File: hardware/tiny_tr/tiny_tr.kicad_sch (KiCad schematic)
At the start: 10 parts, among them U1 ATtiny85-20P, U2 PAM8302AAD

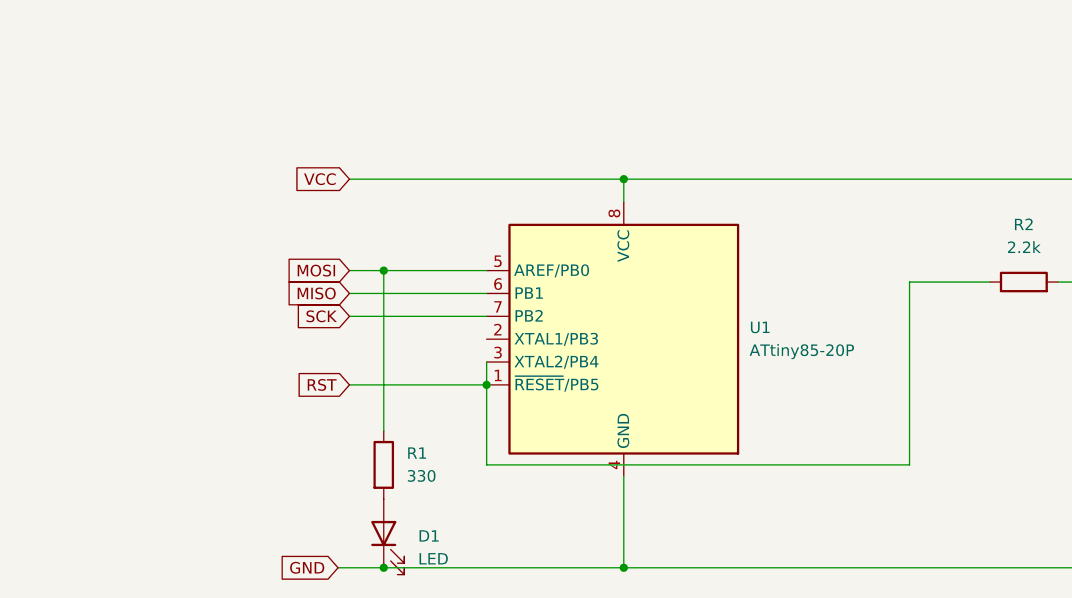
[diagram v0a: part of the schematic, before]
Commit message: feat(hardware): Create schematic based on current circuit
Co-Authored-By: Claude Sonnet 4.5 <noreply@anthropic.com>
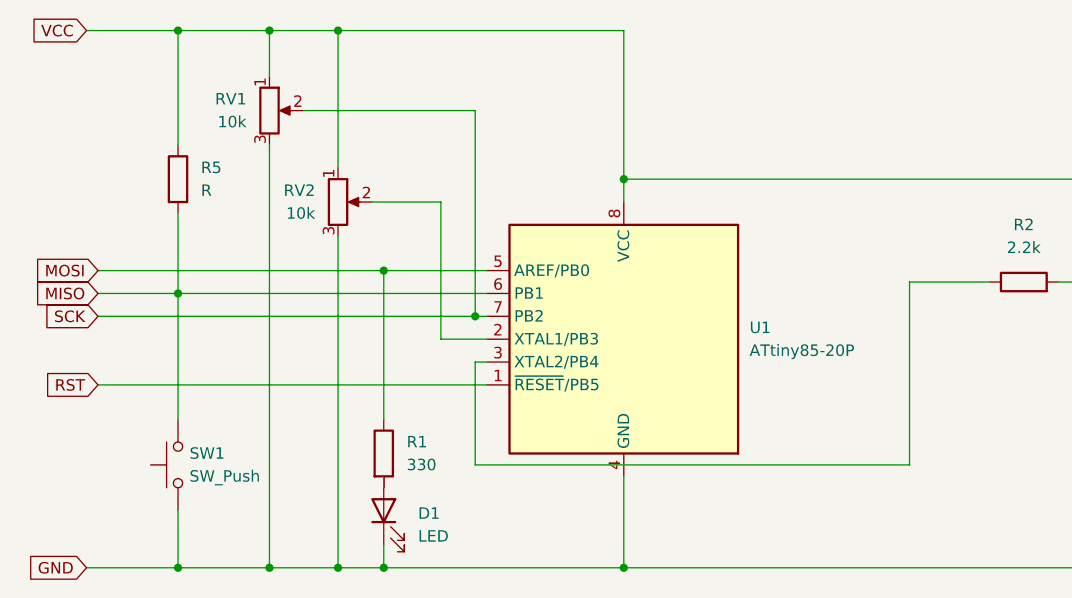
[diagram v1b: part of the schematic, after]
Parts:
- added R5: R, symbol Device:R
- added RV1, RV2: 10k, symbol Device:R_Potentiometer
- added SW1: SW_Push, symbol Switch:SW_Push
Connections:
- net GND: now also RV1.3, RV2.3, SW1.1
- net MISO: now also R5.2, SW1.2
- net RST: no longer R2.1, U1.3 (XTAL2/PB4)
- net SCK: now also RV1.2
- net VCC: now also R5.1, RV1.1, RV2.1
- net at U1.2 (XTAL1/PB3): now also RV2.2
- new net: R2.1, U1.3 (XTAL2/PB4)
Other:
- moved on the sheet: D1, R1

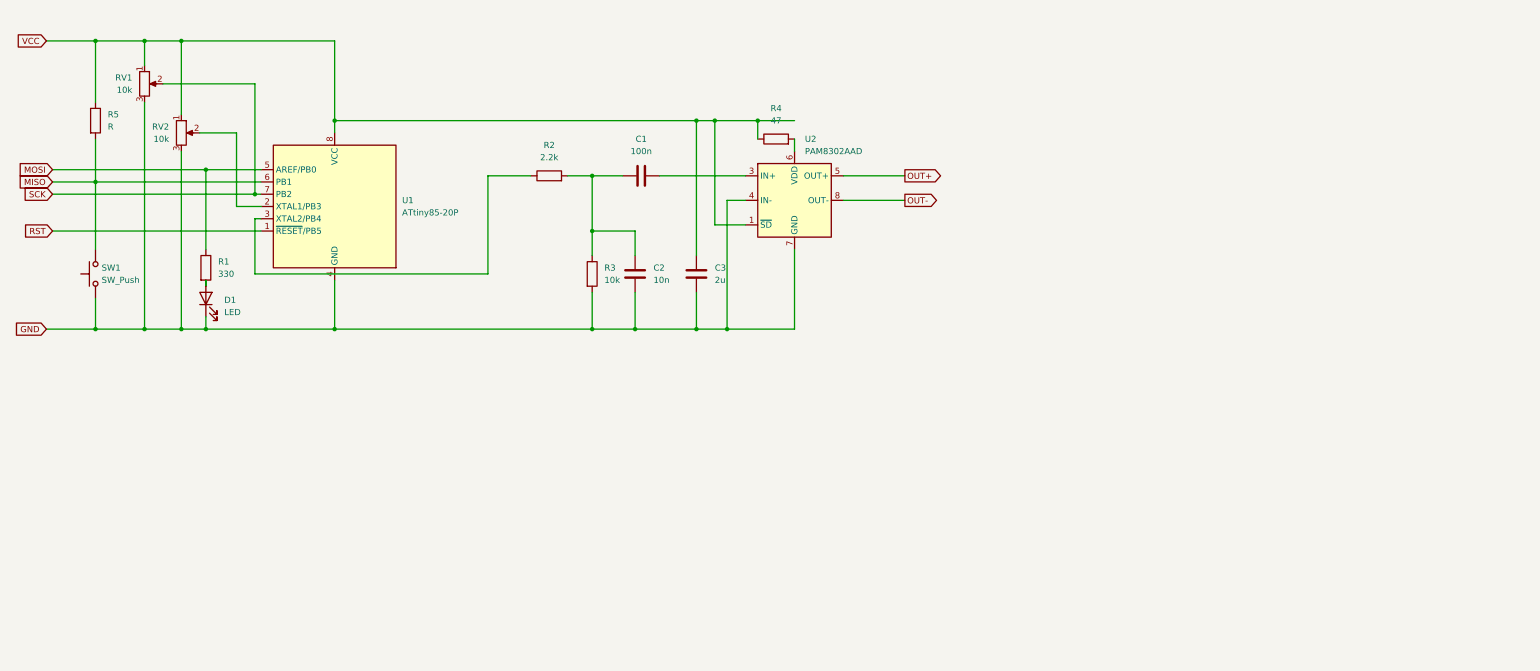
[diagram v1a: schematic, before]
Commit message: fix(hardware): Update capacitor values for noise reduction
Co-Authored-By: Claude Opus 4.5 <noreply@anthropic.com>
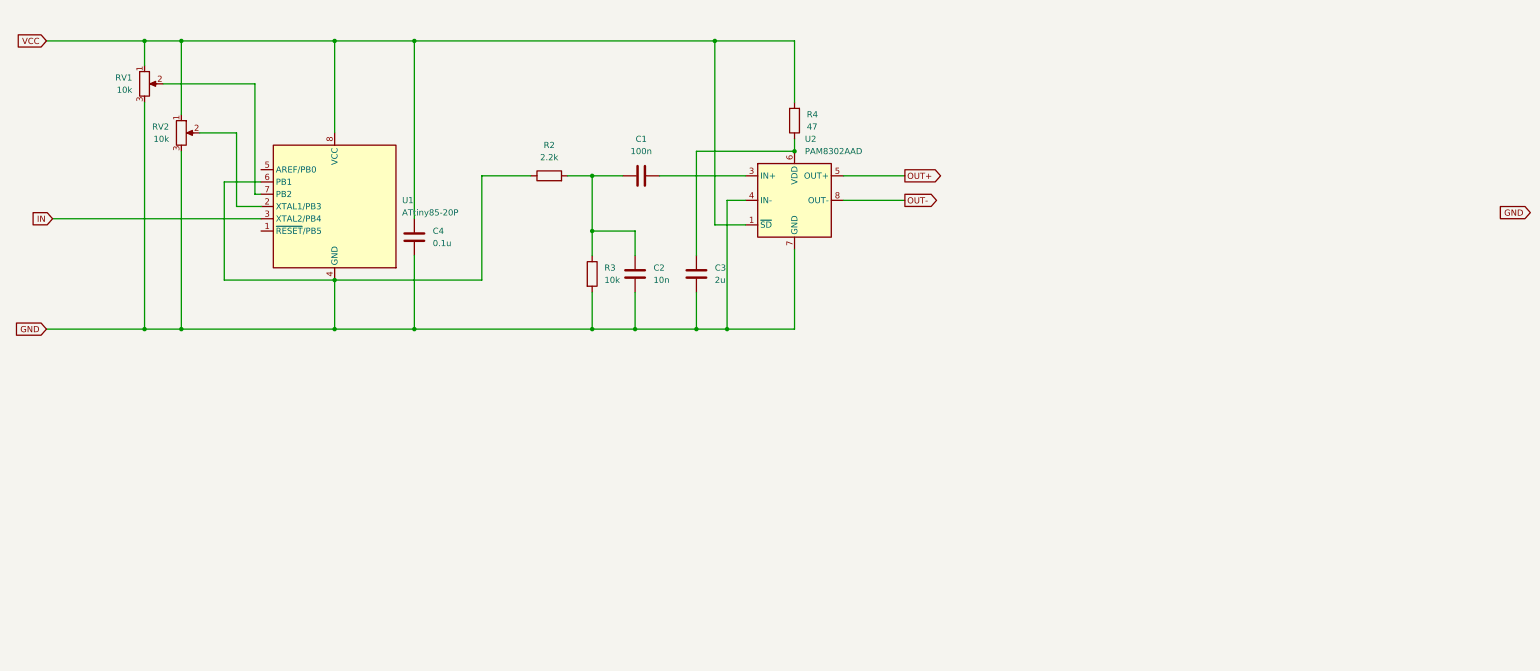
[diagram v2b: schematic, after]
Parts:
- removed D1: LED, symbol Device:LED
- removed R1: 330, symbol Device:R
- removed R5: R, symbol Device:R
- removed SW1: SW_Push, symbol Switch:SW_Push
- added C4: 0.1u, symbol Device:C
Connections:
- net MISO is gone; now on net GND: U1.6 (PB1)
- net GND: now also R2.1, C4.2
- net VCC: now also R4.2, C4.1; no longer C3.1, R4.1
- net IN: now reaches U1.3 (XTAL2/PB4)
- net IN: no longer R2.1
- net at U2.6 (VDD): now also C3.1, R4.1; no longer R4.2
- net MOSI: no longer names the net of U1.5 (AREF/PB0)
- net RST: no longer names the net of U1.1 (~{RESET}/PB5)
- net SCK: no longer names the net of RV1.2, U1.7 (PB2)
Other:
- moved on the sheet: R4

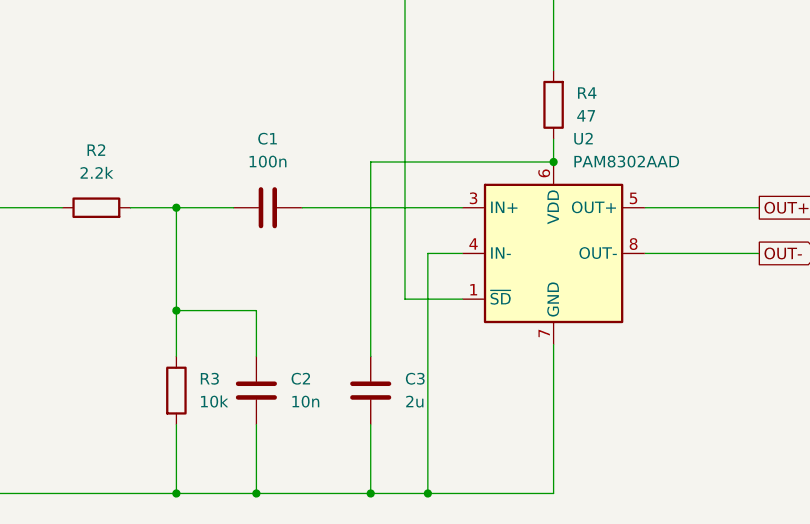
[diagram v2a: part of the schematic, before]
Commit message: fix(hardware): Increase PAM8302 bypass capacitor to 100uF
Prevents voltage droop during kick attack that was causing
power rail fluctuations.

Co-Authored-By: Claude Opus 4.5 <noreply@anthropic.com>
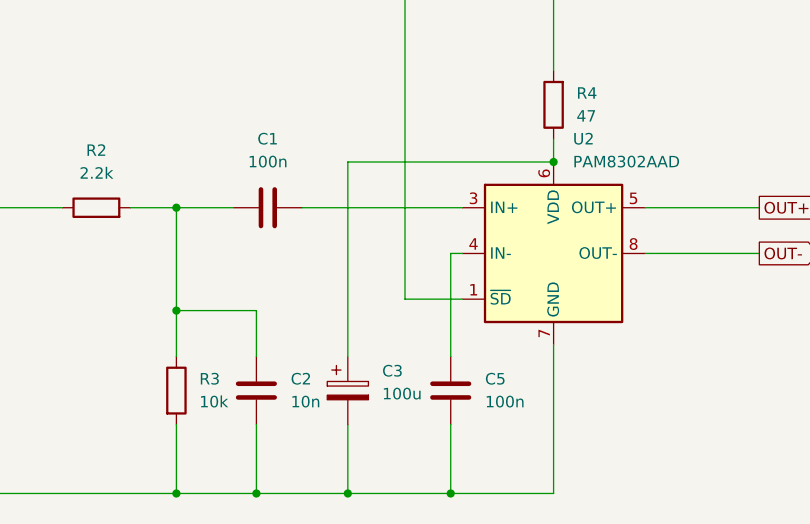
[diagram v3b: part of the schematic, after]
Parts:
- removed C3: 2u, symbol Device:C
- added C3: 100u, symbol Device:C_Polarized
- added C5: 100n, symbol Device:C
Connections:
- net GND: now also C3.2, C5.2; no longer U2.4 (IN-)
- net at R4.1, U2.6 (VDD): now also C3.1
- new net: C5.1, U2.4 (IN-)
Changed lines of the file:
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@@
-	)
-	(junction
-		(at 162.56 92.71)
-		(diameter 0)
-		(color 0 0 0 0)
 	)
 	(junction
@@
 	)
 	(junction
-		(at 156.21 92.71)
+		(at 41.91 33.02)
 		(diameter 0)
 		(color 0 0 0 0)
 	)
 	(junction
-		(at 41.91 33.02)
+		(at 165.1 92.71)
 		(diameter 0)
 		(color 0 0 0 0)
@@
 	)
 	(junction
+		(at 153.67 92.71)
+		(diameter 0)
+		(color 0 0 0 0)
+	)
+	(junction
 		(at 176.53 55.88)
 		(diameter 0)
@@
 	(wire
 		(pts
-			(xy 162.56 66.04) (xy 162.56 92.71)
+			(xy 165.1 66.04) (xy 165.1 77.47)
+		)
+		(stroke
+			(width 0)
+			(type default)
+		)
+	)
+	(wire
+		(pts
+			(xy 165.1 92.71) (xy 176.53 92.71)
 		)
 		(stroke
@@
 	(wire
 		(pts
-			(xy 156.21 85.09) (xy 156.21 92.71)
+			(xy 153.67 85.09) (xy 153.67 92.71)
 		)
 		(stroke
@@
 	(wire
 		(pts
+			(xy 153.67 55.88) (xy 153.67 77.47)
+		)
+		(stroke
+			(width 0)
+			(type default)
+		)
+	)
+	(wire
+		(pts
 			(xy 49.53 33.02) (xy 81.28 33.02)
 		)
@@
 	(wire
 		(pts
-			(xy 156.21 55.88) (xy 176.53 55.88)
+			(xy 153.67 55.88) (xy 176.53 55.88)
 		)
 		(stroke
@@
 	(wire
 		(pts
-			(xy 143.51 92.71) (xy 156.21 92.71)
+			(xy 143.51 92.71) (xy 153.67 92.71)
 		)
 		(stroke
@@
 	(wire
 		(pts
+			(xy 153.67 92.71) (xy 165.1 92.71)
+		)
+		(stroke
+			(width 0)
+			(type default)
+		)
+	)
+	(wire
+		(pts
 			(xy 97.79 33.02) (xy 97.79 69.85)
 		)
@@
 	(wire
 		(pts
-			(xy 166.37 66.04) (xy 162.56 66.04)
+			(xy 166.37 66.04) (xy 165.1 66.04)
 		)
 		(stroke
@@
 	(wire
 		(pts
+			(xy 165.1 85.09) (xy 165.1 92.71)
+		)
+		(stroke
+			(width 0)
+			(type default)
+		)
+	)
+	(wire
+		(pts
 			(xy 45.72 41.91) (xy 64.77 41.91)
 		)
@@
 	(wire
 		(pts
-			(xy 156.21 92.71) (xy 162.56 92.71)
-		)
-		(stroke
-			(width 0)
-			(type default)
-		)
-	)
-	(wire
-		(pts
-			(xy 162.56 92.71) (xy 176.53 92.71)
-		)
-		(stroke
-			(width 0)
-			(type default)
-		)
-	)
-	(wire
-		(pts
 			(xy 148.59 60.96) (xy 166.37 60.96)
-		)
-		(stroke
-			(width 0)
-			(type default)
-		)
-	)
-	(wire
-		(pts
-			(xy 156.21 55.88) (xy 156.21 77.47)
 		)
 		(stroke
@@
 	)
 	(symbol
+		(lib_id "Device:C")
+		(at 165.1 81.28 0)
+		(unit 1)
+		(exclude_from_sim no)
+		(in_bom yes)
+		(on_board yes)
+		(dnp no)
+		(fields_autoplaced yes)
+		(property "Reference" "C5"
+			(at 168.91 80.0099 0)
+			(effects
+				(font
+					(size 1.27 1.27)
+				)
+				(justify left)
+			)
+		)
+		(property "Value" "100n"
+			(at 168.91 82.5499 0)
+			(effects
+				(font
+					(size 1.27 1.27)
+				)
+				(justify left)
+			)
+		)
+		(property "Footprint" ""
+			(at 166.0652 85.09 0)
+			(effects
+				(font
+					(size 1.27 1.27)
+				)
+				(hide yes)
+			)
+		)
+		(property "Datasheet" "~"
+			(at 165.1 81.28 0)
+			(effects
+				(font
+					(size 1.27 1.27)
+				)
+				(hide yes)
+			)
+		)
+		(property "Description" "Unpolarized capacitor"
+			(at 165.1 81.28 0)
+			(effects
+				(font
+					(size 1.27 1.27)
+				)
+				(hide yes)
+			)
+		)
+		(pin "1"
+		)
+		(pin "2"
+		)
+		(instances
+			(project ""
+				(path "/b0a62a77-cbdd-43ac-b9b7-6d13322499f8"
+					(reference "C5")
+					(unit 1)
+				)
+			)
+		)
+	)
+	(symbol
 		(lib_id "Device:R")
 		(at 134.62 81.28 0)
@@
 				(path "/b0a62a77-cbdd-43ac-b9b7-6d13322499f8"
 					(reference "R3")
-					(unit 1)
-				)
-			)
-		)
-	)
-	(symbol
-		(lib_id "Device:C")
-		(at 156.21 81.28 0)
-		(unit 1)
-		(exclude_from_sim no)
-		(in_bom yes)
-		(on_board yes)
-		(dnp no)
-		(fields_autoplaced yes)
-		(property "Reference" "C3"
-			(at 160.02 80.0099 0)
-			(effects
-				(font
-					(size 1.27 1.27)
-				)
-				(justify left)
-			)
-		)
-		(property "Value" "2u"
-			(at 160.02 82.5499 0)
-			(effects
-				(font
-					(size 1.27 1.27)
-				)
-				(justify left)
-			)
-		)
-		(property "Footprint" ""
-			(at 157.1752 85.09 0)
-			(effects
-				(font
-					(size 1.27 1.27)
-				)
-				(hide yes)
-			)
-		)
-		(property "Datasheet" "~"
-			(at 156.21 81.28 0)
-			(effects
-				(font
-					(size 1.27 1.27)
-				)
-				(hide yes)
-			)
-		)
-		(property "Description" "Unpolarized capacitor"
-			(at 156.21 81.28 0)
-			(effects
-				(font
-					(size 1.27 1.27)
-				)
-				(hide yes)
-			)
-		)
-		(pin "1"
-		)
-		(pin "2"
-		)
-		(instances
-			(project ""
-				(path "/b0a62a77-cbdd-43ac-b9b7-6d13322499f8"
-					(reference "C3")
 					(unit 1)
 				)
@@
 					(unit 1)
 				)
+			)
+		)
+	)
+	(symbol
+		(lib_id "Device:C_Polarized")
+		(at 153.67 81.28 0)
+		(unit 1)
+		(exclude_from_sim no)
+		(in_bom yes)
+		(on_board yes)
+		(dnp no)
+		(fields_autoplaced yes)
+		(property "Reference" "C3"
+			(at 157.48 79.1209 0)
+			(effects
+				(font
+					(size 1.27 1.27)
+				)
+				(justify left)
+			)
+		)
+		(property "Value" "100u"
+			(at 157.48 81.6609 0)
+			(effects
+				(font
+					(size 1.27 1.27)
+				)
+				(justify left)
+			)
+		)
+		(property "Footprint" ""
+			(at 154.6352 85.09 0)
+			(effects
+				(font
+					(size 1.27 1.27)
+				)
+				(hide yes)
+			)
+		)
+		(property "Datasheet" "~"
+			(at 153.67 81.28 0)
+			(effects
+				(font
+					(size 1.27 1.27)
+				)
+				(hide yes)
+			)
+		)
+		(property "Description" "Polarized capacitor"
+			(at 153.67 81.28 0)
+			(effects
+				(font
+					(size 1.27 1.27)
+				)
+				(hide yes)
+			)
+		)
+		(pin "1"
+		)
+		(pin "2"
+		)
+		(instances
+			(project ""
+				(path "/b0a62a77-cbdd-43ac-b9b7-6d13322499f8"
+					(reference "C3")
+					(unit 1)
+				)

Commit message: feat(hardware): Add voice selection button on PB0
- Add button connected to pin 5 (PB0) with internal pull-up
- Remove unnecessary external pull-up resistor

Co-Authored-By: Claude Opus 4.5 <noreply@anthropic.com>
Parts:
- added SW1: SW_Push, symbol Switch:SW_Push
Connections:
- net GND: now also SW1.1
- net at U1.5 (AREF/PB0): now also SW1.2
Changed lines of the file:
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@@
+	)
+	(junction
+		(at 53.34 92.71)
+		(diameter 0)
+		(color 0 0 0 0)
 	)
 	(junction
@@
 	(wire
 		(pts
+			(xy 53.34 92.71) (xy 81.28 92.71)
+		)
+		(stroke
+			(width 0)
+			(type default)
+		)
+	)
+	(wire
+		(pts
 			(xy 21.59 92.71) (xy 41.91 92.71)
 		)
@@
 	(wire
 		(pts
+			(xy 53.34 87.63) (xy 53.34 92.71)
+		)
+		(stroke
+			(width 0)
+			(type default)
+		)
+	)
+	(wire
+		(pts
 			(xy 165.1 92.71) (xy 176.53 92.71)
 		)
@@
 	(wire
 		(pts
+			(xy 53.34 59.69) (xy 53.34 77.47)
+		)
+		(stroke
+			(width 0)
+			(type default)
+		)
+	)
+	(wire
+		(pts
 			(xy 64.77 64.77) (xy 66.04 64.77)
 		)
@@
 	(wire
 		(pts
-			(xy 49.53 92.71) (xy 81.28 92.71)
+			(xy 49.53 92.71) (xy 53.34 92.71)
 		)
 		(stroke
@@
 		(pts
 			(xy 58.42 62.23) (xy 58.42 82.55)
+		)
+		(stroke
+			(width 0)
+			(type default)
+		)
+	)
+	(wire
+		(pts
+			(xy 66.04 59.69) (xy 53.34 59.69)
 		)
 		(stroke
@@
 					(unit 1)
 				)
+			)
+		)
+	)
+	(symbol
+		(lib_id "Switch:SW_Push")
+		(at 53.34 82.55 90)
+		(unit 1)
+		(exclude_from_sim no)
+		(in_bom yes)
+		(on_board yes)
+		(dnp no)
+		(fields_autoplaced yes)
+		(property "Reference" "SW1"
+			(at 54.61 81.2799 90)
+			(effects
+				(font
+					(size 1.27 1.27)
+				)
+				(justify right)
+			)
+		)
+		(property "Value" "SW_Push"
+			(at 54.61 83.8199 90)
+			(effects
+				(font
+					(size 1.27 1.27)
+				)
+				(justify right)
+			)
+		)
+		(property "Footprint" ""
+			(at 48.26 82.55 0)
+			(effects
+				(font
+					(size 1.27 1.27)
+				)
+				(hide yes)
+			)
+		)
+		(property "Datasheet" "~"
+			(at 48.26 82.55 0)
+			(effects
+				(font
+					(size 1.27 1.27)
+				)
+				(hide yes)
+			)
+		)
+		(property "Description" "Push button switch, generic, two pins"
+			(at 53.34 82.55 0)
+			(effects
+				(font
+					(size 1.27 1.27)
+				)
+				(hide yes)
+			)
+		)
+		(pin "2"
+		)
+		(pin "1"
+		)
+		(instances
+			(project ""
+				(path "/b0a62a77-cbdd-43ac-b9b7-6d13322499f8"
+					(reference "SW1")
+					(unit 1)
+				)

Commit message: feat(hardware): Add sequencer circuit to schematic
Co-Authored-By: Claude Opus 4.5 <noreply@anthropic.com>
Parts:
- added C6: 100n, symbol Device:C
- added D1: LED, symbol Device:LED
- added J1: Conn_01x02_Socket, symbol Connector:Conn_01x02_Socket
- added R1: 330, symbol Device:R
- added R5: 2.2k, symbol Device:R
- added R6: 4.7k, symbol Device:R
- added R7: 10k, symbol Device:R
- added SW2, SW3, SW4: SW_Push, symbol Switch:SW_Push
- added U3: ATtiny85-20P, Package_DIP:DIP-8_W7.62mm, symbol MCU_Microchip_ATtiny:ATtiny85-20P
- R4: value 47 -> 10k
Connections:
- net GND: now also C6.2, D1.1 (K), SW2.1, SW3.1, SW4.1, U3.4 (GND); no longer R2.1, U1.6 (PB1)
- net VCC: now also C3.1, R4.1, U2.6 (VDD), U3.8 (VCC); no longer R4.2
- net IN renamed CV
- net OUT+: no longer names the net of U2.5 (OUT+)
- net OUT+: now also J1.1 (Pin_1)
- net OUT-: no longer names the net of U2.8 (OUT-)
- net OUT-: now also J1.2 (Pin_2)
- new net: C6.1, R7.2
- new net: R1.1, U3.6 (PB1)
- new net: D1.2 (A), R1.2
- new net: R2.1, U1.6 (PB1)
- new net: R6.2, SW4.2
- new net: R4.2, R5.1, R6.1, R7.1, SW2.2, U3.2 (XTAL1/PB3)
- new net: R5.2, SW3.2
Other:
- moved on the sheet: C1, C2, C3, C4, C5, R2, R3, RV1, RV2, SW1, U1, U2
